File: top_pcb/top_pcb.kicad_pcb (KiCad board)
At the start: 2 copper layers, 50 x 50 mm, 14 parts, among them J1 flat_cable_connector, J2 header, J3 free_holes

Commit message: Change connector position on top_pcb
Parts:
- moved J1 2.80 mm to (139.5, 75.0)
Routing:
- net GND: track 177.1 -> 79.2 mm, vias 4 -> 2
- net G17: track 64.2 -> 10.6 mm, vias 0 -> 1
- net G26: track 51.6 -> 19.1 mm
- net G0: track 22.3 -> 48.7 mm
- net RST: track 23.5 -> 39.0 mm
- net G25: track 43.8 -> 47.1 mm
- net G22: track 19.9 -> 17.1 mm
- net G16: track 18.6 -> 15.7 mm
- net G21: track 19.0 -> 16.4 mm
- net G5: track 20.6 -> 18.1 mm
- net G19: track 21.2 -> 19.0 mm, vias 0 -> 1
- net G35: track 28.9 -> 27.1 mm
- net G36: track 24.7 -> 23.1 mm
- net G3: track 14.7 -> 16.4 mm, vias 1 -> 0
- net G18: track 19.8 -> 18.2 mm, vias 0 -> 1
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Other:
- board text added: "Rev 2019.06"
- board text removed: "MI"
- board text removed: "MO"
- board text removed: "OUT"
- board text removed: "R0"
- board text removed: "R2"
- board text removed: "Rev 2019.05"
- board text removed: "SCK"
- board text removed: "SDA"
- board text removed: "SK"

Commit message: Assign corner edge to top_pcb
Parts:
- added corner1: corner_edge, footprints:corner_edge, F.Cu at (150.0, 50.0)
- added corner2: corner_edge, footprints:corner_edge, B.Cu at (150.0, 100.0)
- added corner3: corner_edge, footprints:corner_edge, B.Cu at (100.0, 50.0)
- added corner4: corner_edge, footprints:corner_edge, F.Cu at (100.0, 100.0)
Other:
- outline, holes or cut-outs redrawn
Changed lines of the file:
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@@
-(kicad_pcb (version 20171130) (host pcbnew 5.0.2-bee76a0~70~ubuntu18.04.1)
+(kicad_pcb (version 20171130) (host pcbnew 5.1.2-f72e74a~84~ubuntu18.04.1)
   (general
     (thickness 1.6)
-    (drawings 51)
+    (drawings 47)
     (tracks 374)
     (zones 0)
-    (modules 14)
+    (modules 18)
     (nets 27)
   )
@@
     (zone_45_only no)
     (trace_min 0.2)
-    (segment_width 0.2)
-    (edge_width 0.15)
     (via_size 0.8)
     (via_drill 0.4)
@@
     (uvia_min_size 0.2)
     (uvia_min_drill 0.1)
+    (edge_width 0.15)
+    (segment_width 0.2)
     (pcb_text_width 0.3)
     (pcb_text_size 1.5 1.5)
@@
     (add_net HPWR)
     (add_net RST)
+  )
+  (module footprints:corner_edge (layer F.Cu)
+    (at 100 100 180)
+    (fp_text reference corner4 (at -3.9243 -2.4765) (layer F.SilkS) hide
+      (effects (font (size 1 1) (thickness 0.15)))
+    )
+    (fp_text value corner_edge (at -3.429 -1.4224) (layer F.Fab)
+      (effects (font (size 1 1) (thickness 0.15)))
+    )
+    (fp_line (start 0.6 5) (end 0 5) (layer Edge.Cuts) (width 0.15))
+    (fp_line (start 0.6 2.8) (end 0.6 5) (layer Edge.Cuts) (width 0.15))
+    (fp_arc (start -2.8 2.8) (end 0.6 2.8) (angle -90) (layer Edge.Cuts) (width 0.15))
+    (fp_line (start -8 -0.6) (end -2.8 -0.6) (layer Edge.Cuts) (width 0.15))
+    (fp_line (start -8 0) (end -8 -0.6) (layer Edge.Cuts) (width 0.15))
+  )
+  (module footprints:corner_edge (layer B.Cu)
+    (at 100 50 180)
+    (fp_text reference corner3 (at -3.9243 2.4765) (layer B.SilkS) hide
+      (effects (font (size 1 1) (thickness 0.15)) (justify mirror))
+    )
+    (fp_text value corner_edge (at -3.429 1.4224) (layer B.Fab)
+      (effects (font (size 1 1) (thickness 0.15)) (justify mirror))
+    )
+    (fp_line (start 0.6 -5) (end 0 -5) (layer Edge.Cuts) (width 0.15))
+    (fp_line (start 0.6 -2.8) (end 0.6 -5) (layer Edge.Cuts) (width 0.15))
+    (fp_arc (start -2.8 -2.8) (end 0.6 -2.8) (angle 90) (layer Edge.Cuts) (width 0.15))
+    (fp_line (start -8 0.6) (end -2.8 0.6) (layer Edge.Cuts) (width 0.15))
+    (fp_line (start -8 0) (end -8 0.6) (layer Edge.Cuts) (width 0.15))
+  )
+  (module footprints:corner_edge (layer B.Cu)
+    (at 150 100)
+    (fp_text reference corner2 (at -3.9243 2.4765) (layer B.SilkS) hide
+      (effects (font (size 1 1) (thickness 0.15)) (justify mirror))
+    )
+    (fp_text value corner_edge (at -3.429 1.4224) (layer B.Fab)
+      (effects (font (size 1 1) (thickness 0.15)) (justify mirror))
+    )
+    (fp_line (start 0.6 -5) (end 0 -5) (layer Edge.Cuts) (width 0.15))
+    (fp_line (start 0.6 -2.8) (end 0.6 -5) (layer Edge.Cuts) (width 0.15))
+    (fp_arc (start -2.8 -2.8) (end 0.6 -2.8) (angle 90) (layer Edge.Cuts) (width 0.15))
+    (fp_line (start -8 0.6) (end -2.8 0.6) (layer Edge.Cuts) (width 0.15))
+    (fp_line (start -8 0) (end -8 0.6) (layer Edge.Cuts) (width 0.15))
+  )
+  (module footprints:corner_edge (layer F.Cu)
+    (at 150 50)
+    (fp_text reference corner1 (at -0.4191 -2.6035) (layer F.SilkS) hide
+      (effects (font (size 1 1) (thickness 0.15)))
+    )
+    (fp_text value corner_edge (at -0.0765 -1.6384) (layer F.Fab)
+      (effects (font (size 1 1) (thickness 0.15)))
+    )
+    (fp_line (start 0.6 5) (end 0 5) (layer Edge.Cuts) (width 0.15))
+    (fp_line (start 0.6 2.8) (end 0.6 5) (layer Edge.Cuts) (width 0.15))
+    (fp_arc (start -2.8 2.8) (end 0.6 2.8) (angle -90) (layer Edge.Cuts) (width 0.15))
+    (fp_line (start -8 -0.6) (end -2.8 -0.6) (layer Edge.Cuts) (width 0.15))
+    (fp_line (start -8 0) (end -8 -0.6) (layer Edge.Cuts) (width 0.15))
   )
   (module Symbol:OSHW-Logo_7.5x8mm_SilkScreen (layer F.Cu)
@@
     (effects (font (size 2 2) (thickness 0.5)))
   )
-  (gr_line (start 150 52.2) (end 150 97.8) (layer Edge.Cuts) (width 0.2))
+  (gr_line (start 150 55) (end 150 95) (layer Edge.Cuts) (width 0.2))
   (gr_text 34 (at 129.9337 87.5284 270) (layer B.SilkS)
     (effects (font (size 1 1) (thickness 0.25)) (justify mirror))
@@
     (effects (font (size 0.7 0.7) (thickness 0.175)) (justify mirror))
   )
-  (gr_line (start 102.2 50) (end 100 52.2) (layer Edge.Cuts) (width 0.15))
-  (gr_line (start 100 97.8) (end 100 52.2) (layer Edge.Cuts) (width 0.15))
-  (gr_line (start 102.2 100) (end 100 97.8) (layer Edge.Cuts) (width 0.15))
-  (gr_line (start 147.8 100) (end 102.2 100) (layer Edge.Cuts) (width 0.15))
-  (gr_line (start 150 97.8) (end 147.8 100) (layer Edge.Cuts) (width 0.15))
-  (gr_line (start 147.8 50) (end 150 52.2) (layer Edge.Cuts) (width 0.15))
-  (gr_line (start 102.2 50) (end 147.8 50) (layer Edge.Cuts) (width 0.15))
+  (gr_line (start 100 95) (end 100 55) (layer Edge.Cuts) (width 0.15))
+  (gr_line (start 142 100) (end 108 100) (layer Edge.Cuts) (width 0.15))
+  (gr_line (start 108 50) (end 142 50) (layer Edge.Cuts) (width 0.15))
   (segment (start 137.65 68.25) (end 138.6253 68.25) (width 0.25) (layer B.Cu) (net 1))
   (segment (start 138.6253 68.25) (end 138.6253 69.1131) (width 0.25) (layer B.Cu) (net 1))

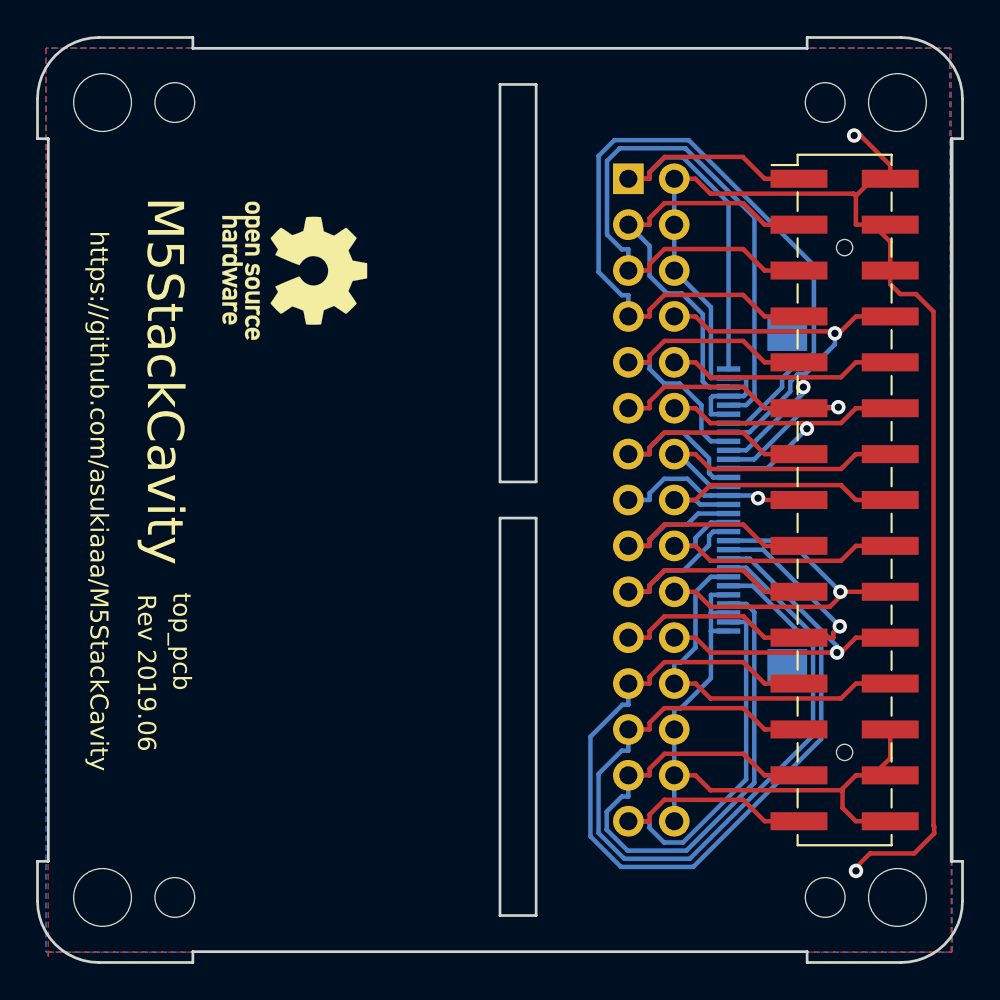
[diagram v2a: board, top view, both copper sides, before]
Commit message: Add hole to top_pcb
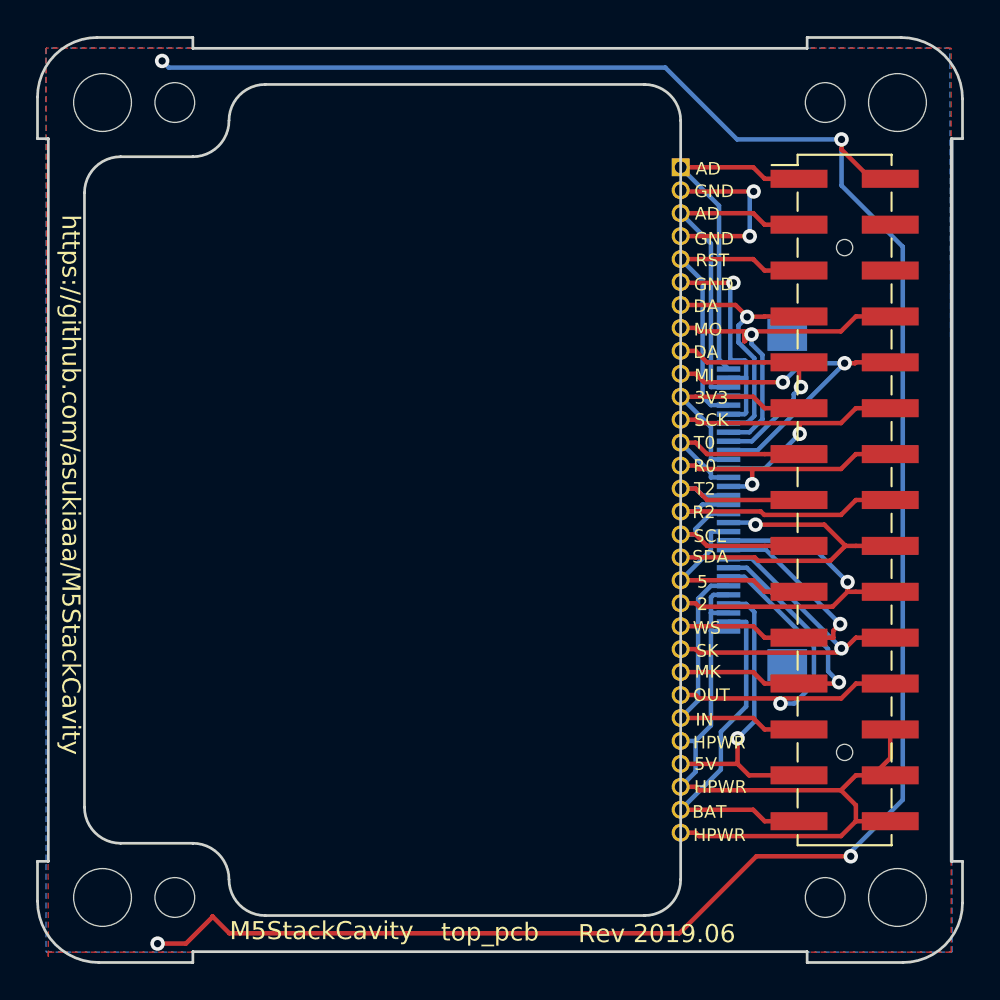
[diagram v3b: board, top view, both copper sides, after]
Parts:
- removed CUTREF1, CUTREF2: hole_to_cut, footprints:hole_to_cut
- J3: footprint footprints:PinHeader_2x15_P2.54mm_Vertical_without_silks -> footprints:PinHeader_1x30_P1.27mm_Vertical_without_silks
- OSHWREF2: moved to B.Cu
- corner1, corner4: value corner_edge -> corner_edge1; footprint footprints:corner_edge -> footprints:corner_edge1
- corner2, corner3: value corner_edge -> corner_edge2; footprint footprints:corner_edge -> footprints:corner_edge2; moved to F.Cu
- moved OSHWREF2 41.1 mm to (144.1, 90.0), turned to 180 degrees
- moved J3 2.96 mm to (135.0, 56.6)
- turned corner2 to 180 degrees
- turned corner3 to 0 degrees
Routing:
- net GND: track 79.2 -> 151.2 mm, vias 2 -> 7
- net G25: track 47.1 -> 14.5 mm, vias 0 -> 1
- net G0: track 48.7 -> 18.5 mm, vias 0 -> 1
- net G34: track 43.6 -> 15.8 mm
- net RST: track 39.0 -> 16.6 mm
- net +5V: track 35.6 -> 17.2 mm, vias 0 -> 1
- net +BATT: track 29.0 -> 19.7 mm
- net +3V3: track 20.1 -> 11.9 mm, vias 1 -> 0
- net G35: track 27.1 -> 19.1 mm
- net G1: track 18.4 -> 10.4 mm
- net HPWR: track 36.1 -> 44.0 mm
- net G22: track 17.1 -> 10.1 mm
- net G5: track 18.1 -> 11.2 mm
- net G26: track 19.1 -> 13.8 mm, vias 0 -> 1
- net G36: track 23.1 -> 18.1 mm
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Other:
- outline, holes or cut-outs redrawn
- board text added: "3."
- board text added: "MI"
- board text added: "MO"
- board text added: "OUT"
- board text added: "R0"
- board text added: "R2"
- board text added: "SCK"
- board text added: "SDA"
- board text added: "SK"

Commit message: Change pad size smaller for pin socket on top_pcb
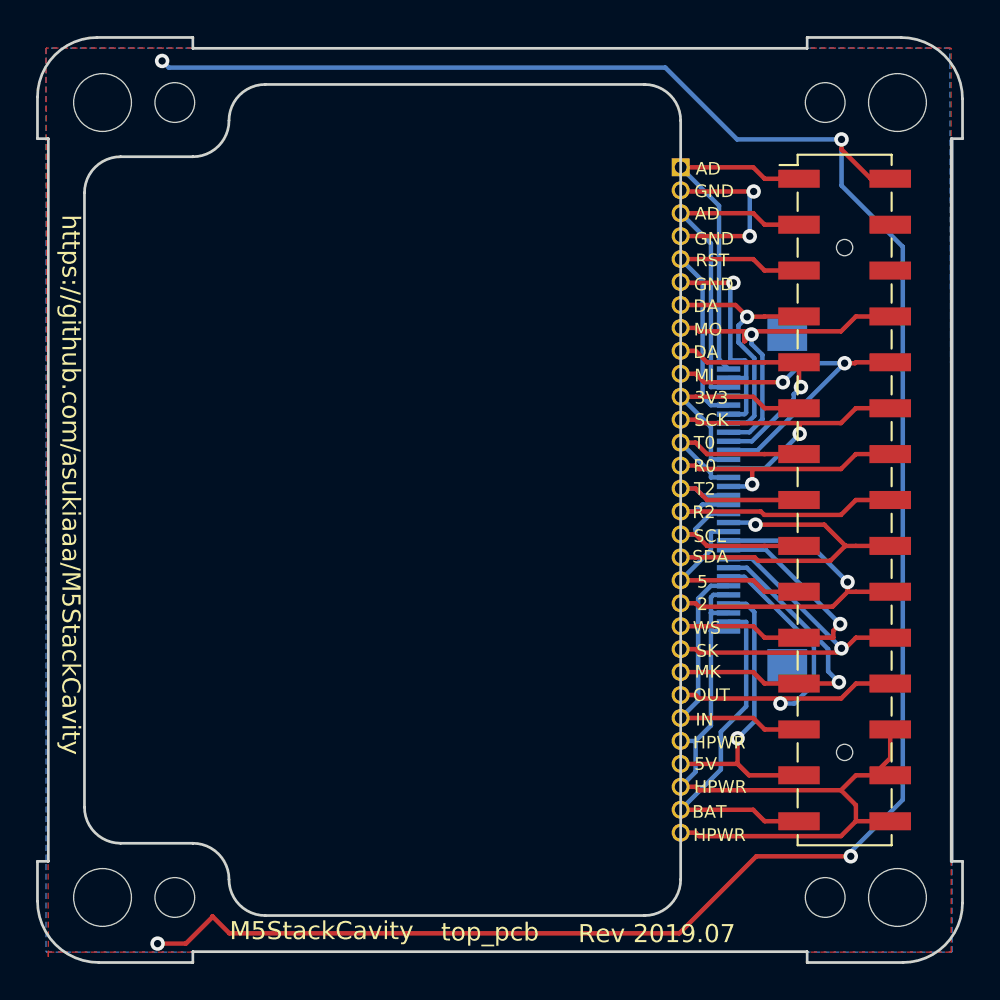
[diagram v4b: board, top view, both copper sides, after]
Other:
- board text added: "Rev 2019.07"
- board text removed: "Rev 2019.06"

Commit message: Rename project name to CavityForM5Stack from M5StackCavity
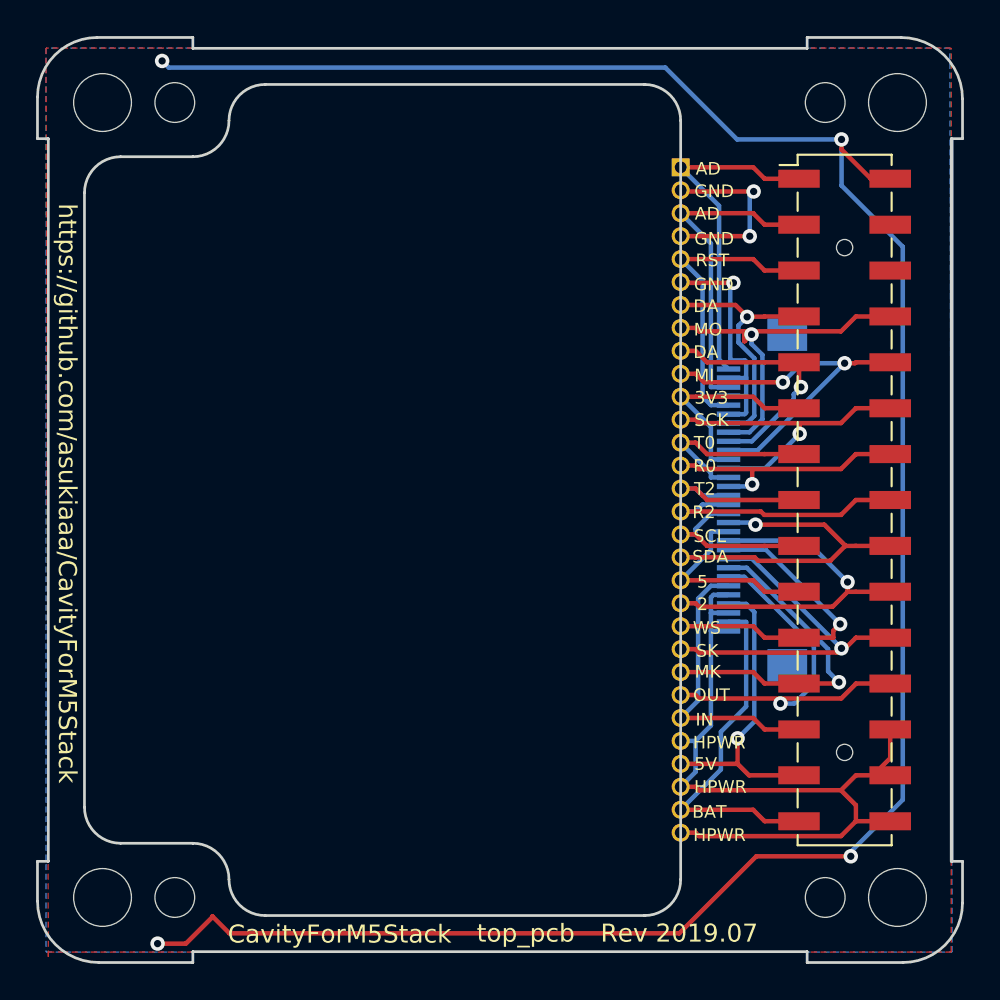
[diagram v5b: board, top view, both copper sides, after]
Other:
- board text added: "CavityForM5Stack"
- board text added: "https://github.com/asukiaaa/CavityForM5Stack"
- board text removed: "https://github.com/asukiaaa/M5StackCavity"
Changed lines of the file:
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@@
-(kicad_pcb (version 20171130) (host pcbnew 5.1.2-f72e74a~84~ubuntu18.04.1)
+(kicad_pcb (version 20171130) (host pcbnew 5.1.4-e60b266~84~ubuntu18.04.1)
   (general
     (thickness 1.6)
@@
     (effects (font (size 1 1) (thickness 0.25)) (justify mirror))
   )
-  (gr_text top_pcb (at 124.4473 98.9203) (layer F.SilkS)
+  (gr_text top_pcb (at 126.4238 98.9832) (layer F.SilkS)
     (effects (font (size 1 1) (thickness 0.25)))
   )
-  (gr_text M5StackCavity (at 115.1255 98.8441) (layer F.SilkS)
+  (gr_text CavityForM5Stack (at 116.1238 99.0332) (layer F.SilkS)
     (effects (font (size 1 1) (thickness 0.25)))
   )
@@
     (effects (font (size 0.7 0.7) (thickness 0.175)) (justify mirror))
   )
-  (gr_text "Rev 2019.07" (at 133.6802 99.0092) (layer F.SilkS)
+  (gr_text "Rev 2019.07" (at 134.9238 98.9832) (layer F.SilkS)
     (effects (font (size 1 1) (thickness 0.25)))
   )
-  (gr_text https://github.com/asukiaaa/M5StackCavity (at 101.2444 74.1553 270) (layer F.SilkS)
+  (gr_text https://github.com/asukiaaa/CavityForM5Stack (at 101.0488 74.6332 270) (layer F.SilkS)
     (effects (font (size 1 1) (thickness 0.25)))
   )
